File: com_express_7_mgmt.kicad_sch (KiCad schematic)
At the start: 66 parts, among them J1 Plug_Bus_CE7_EPT_401-51501-51, Q1 BSS138-7-F, Q2 BSS138-7-F, SW1 SW_1-1825027-1_THT, SW2 SW_1-1825027-1_THT, SW3 SW_DS04-254-1-01BK-SMT, U30 MAX16150A_SOT, U31 74AUP2G132, U32 TPS3840PL30DBVR, U33 74AUP2G132, U34 W25Q32FV_SOIC-8, U35 M24C64-F_DFN8

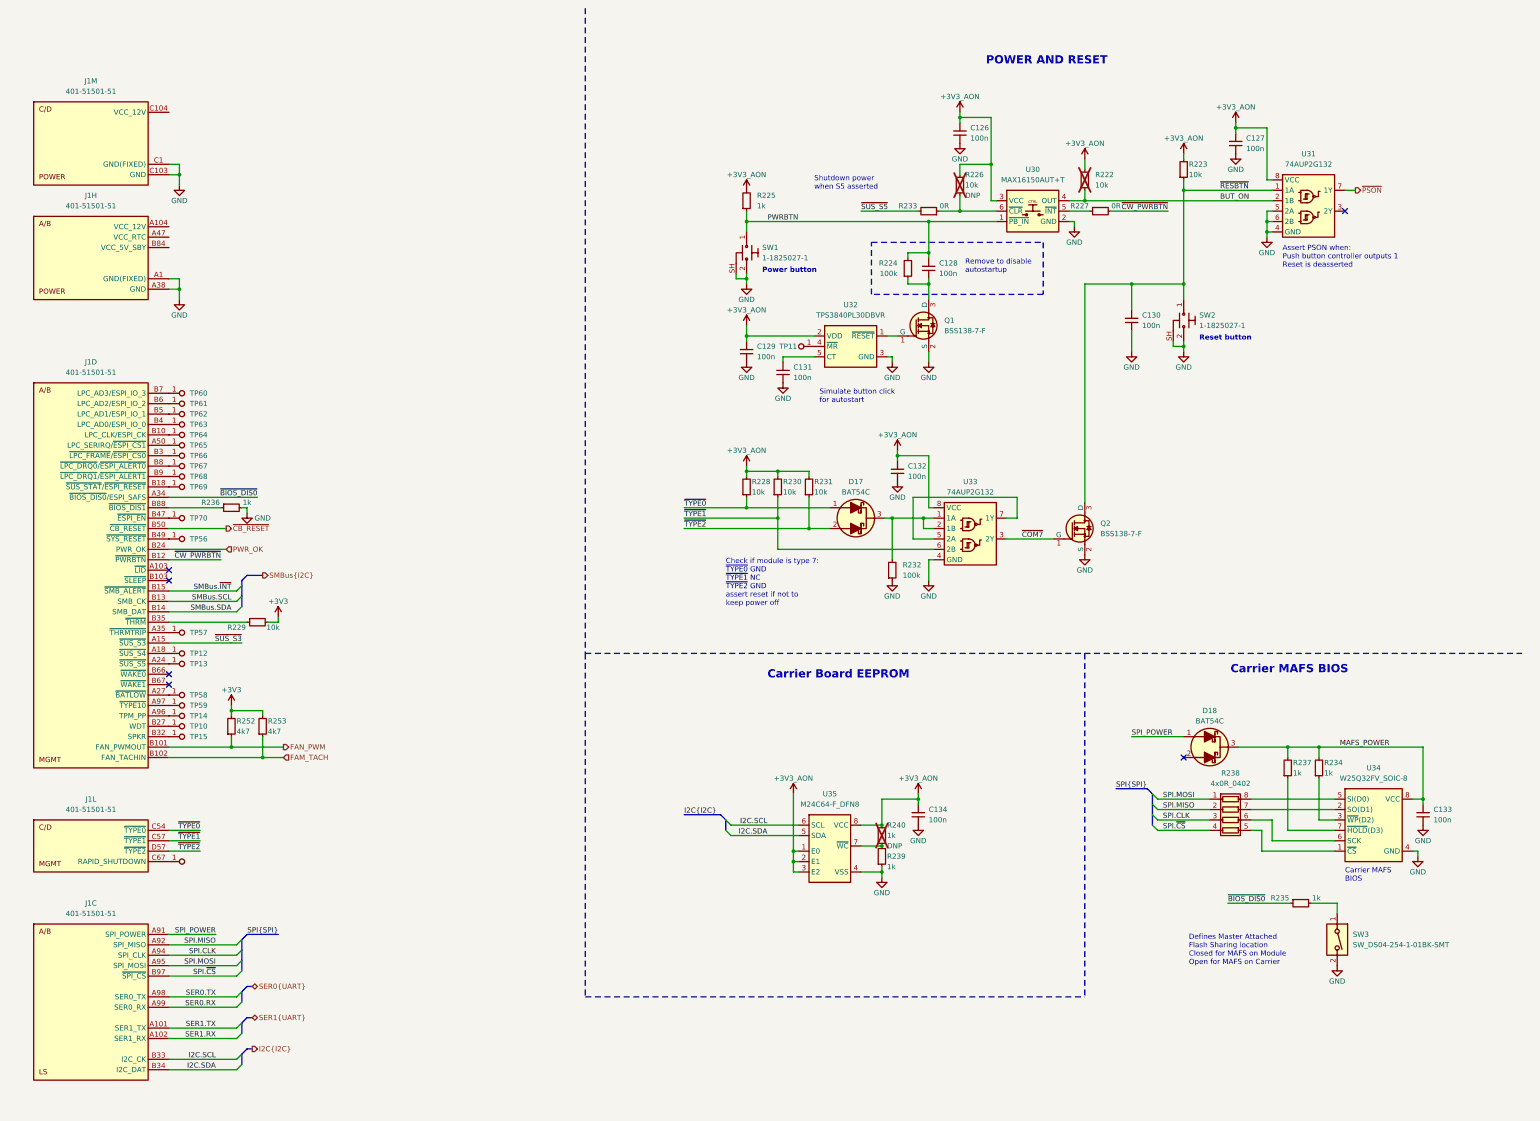
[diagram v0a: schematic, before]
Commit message: [#58137] Update backplane connector pinout
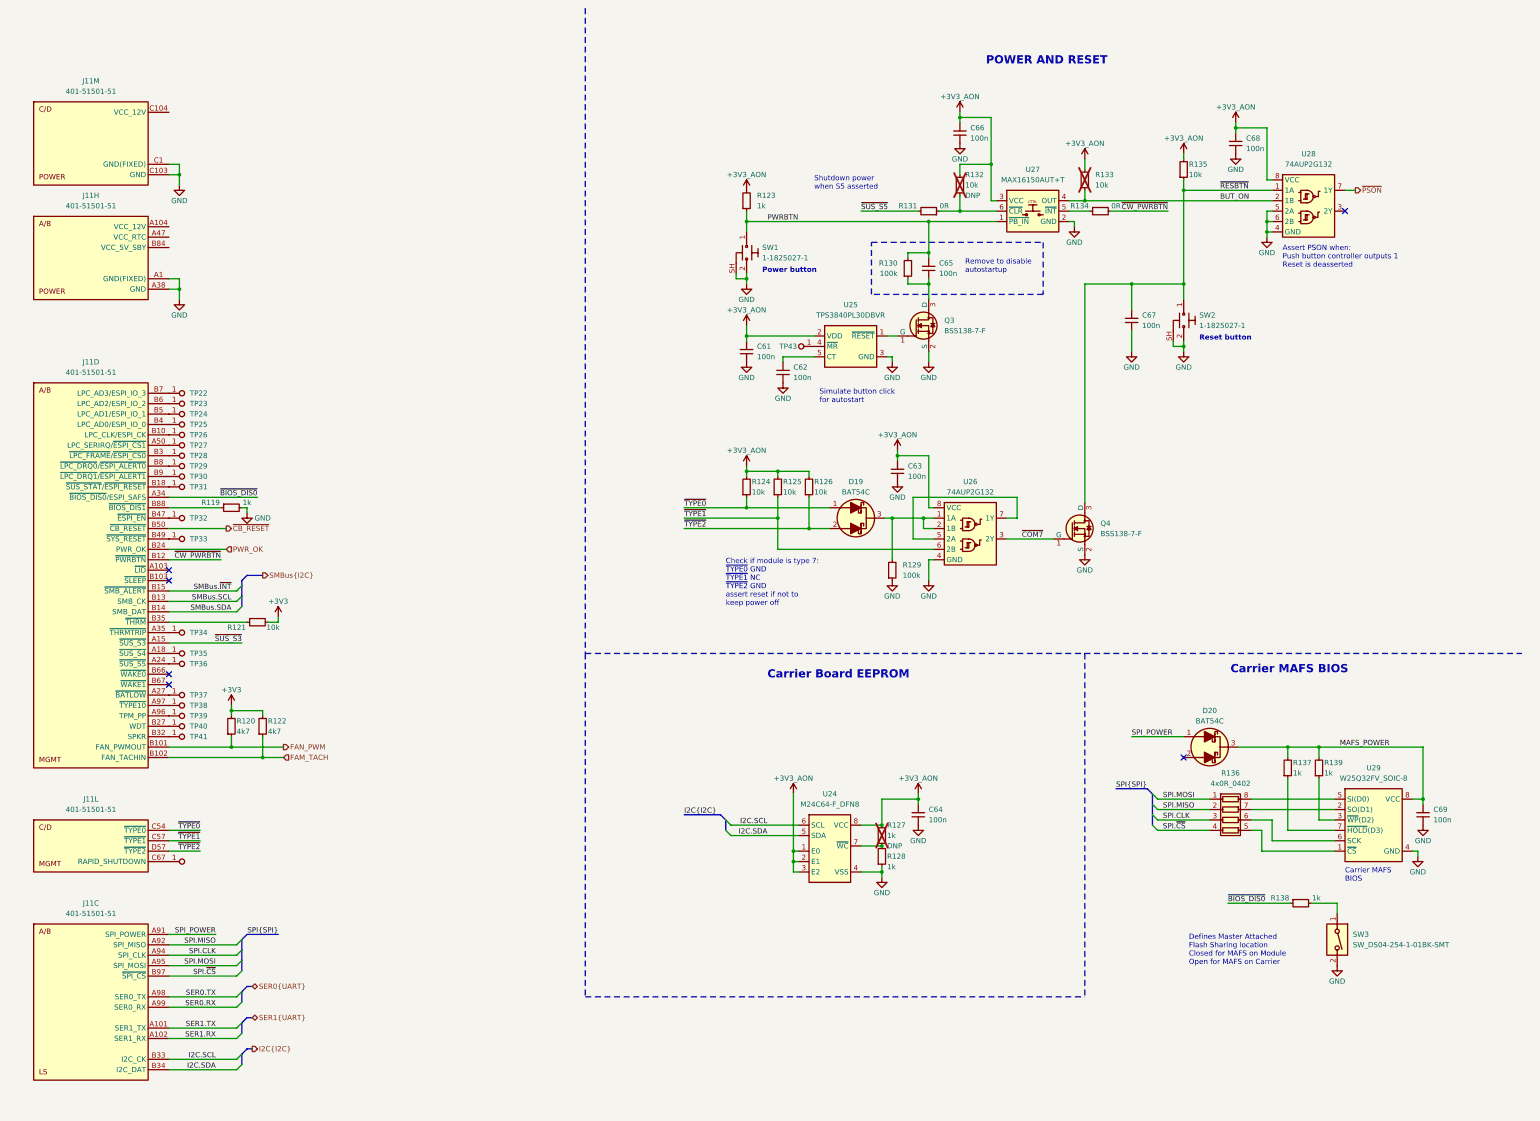
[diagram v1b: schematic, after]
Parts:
- renumbered C129 to C61, C131 to C62, C132 to C63, C134 to C64, C128 to C65, C126 to C66, C130 to C67, C127 to C68, C133 to C69, D17 to D19, D18 to D20, J1 to J11, Q1 to Q3, Q2 to Q4, R236 to R119, R252 to R120, R229 to R121, R253 to R122, R225 to R123, R228 to R124, R230 to R125, R231 to R126, R240 to R127, R239 to R128, R232 to R129, R224 to R130, R233 to R131, R226 to R132, R222 to R133, R227 to R134, R223 to R135, R238 to R136, R237 to R137, R235 to R138, R234 to R139, TP60 to TP22, TP61 to TP23, TP62 to TP24, TP63 to TP25, TP64 to TP26, TP65 to TP27, TP66 to TP28, TP67 to TP29, TP68 to TP30, TP69 to TP31, TP70 to TP32, TP56 to TP33, TP57 to TP34, TP12 to TP35, TP13 to TP36, TP58 to TP37, TP59 to TP38, TP14 to TP39, TP10 to TP40, TP15 to TP41, TP16 to TP42, TP11 to TP43, U35 to U24, U32 to U25, U33 to U26, U30 to U27, U31 to U28, U34 to U29

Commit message: [#58137] Add power sequencing and reset
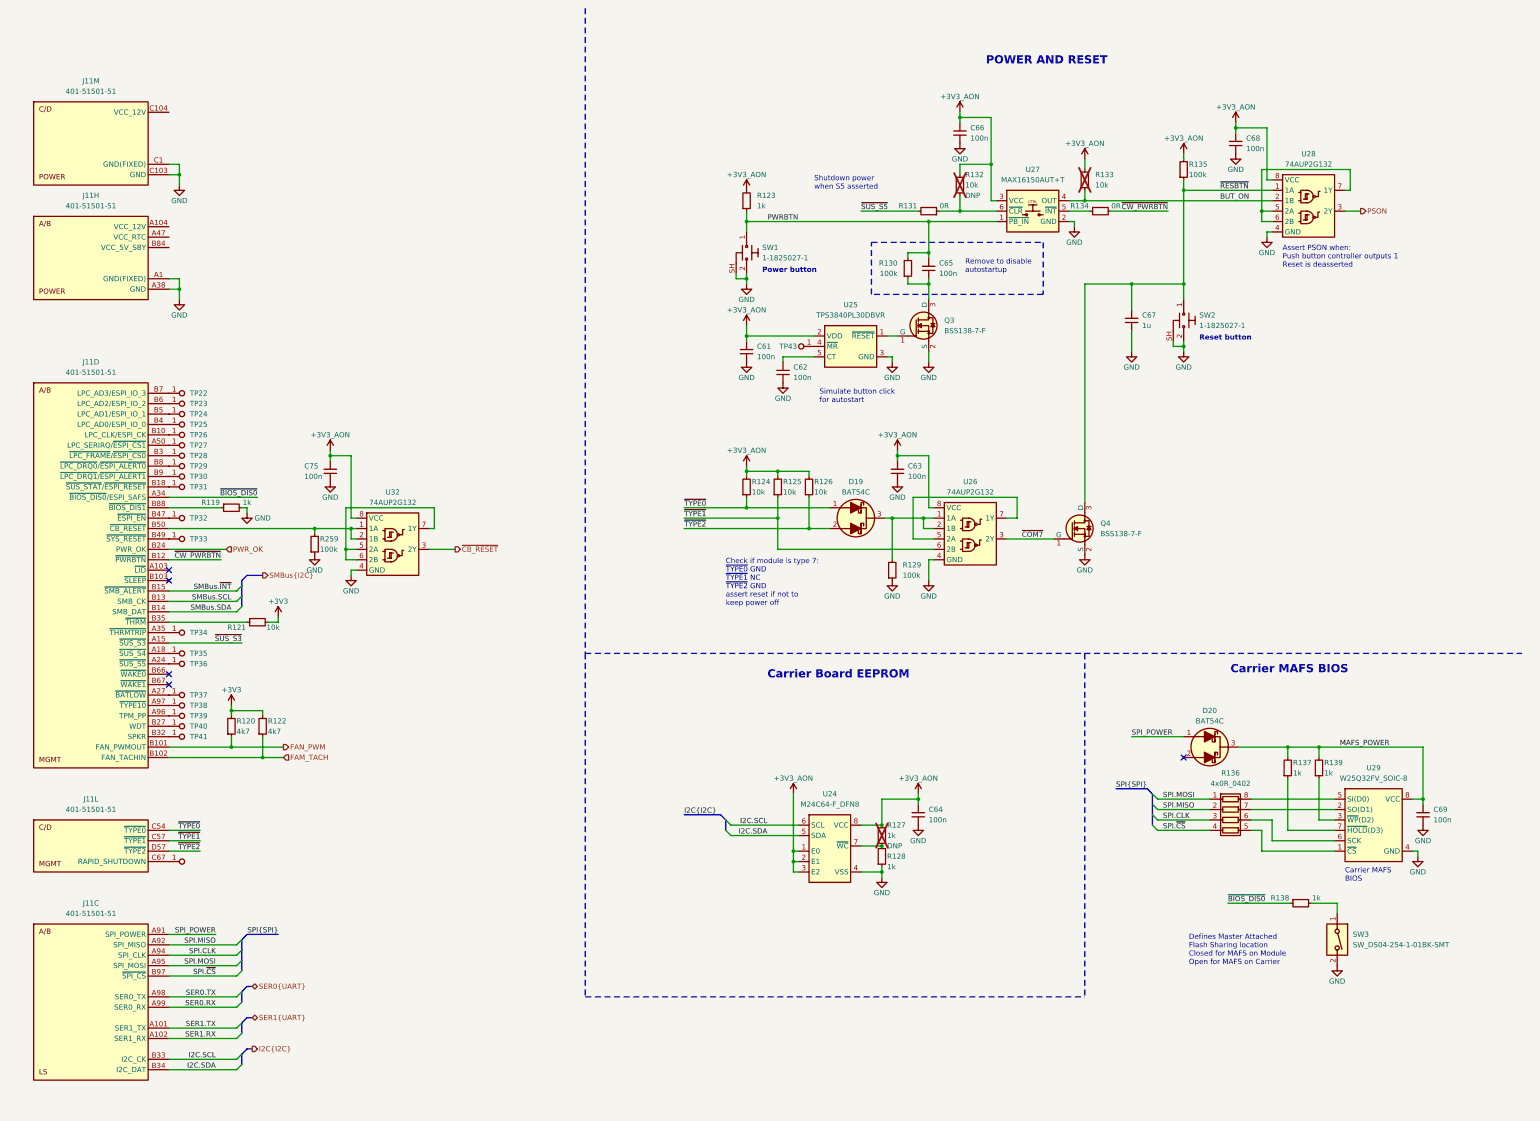
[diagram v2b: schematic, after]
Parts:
- removed C67: C_100n_0402, antmicro-footprints:C_0402_1005Metric, symbol antmicroCapacitors0402:C_100n_0402
- removed R135: R_10k_0402, antmicro-footprints:R_0402_1005Metric, symbol antmicroResistors0402:R_10k_0402
- added C67: C_1u_0402, antmicro-footprints:C_0402_1005Metric, symbol antmicroCapacitors0402:C_1u_0402
- added C75: C_100n_0402, antmicro-footprints:C_0402_1005Metric, symbol antmicroCapacitors0402:C_100n_0402
- added R135, R259: R_100k_0402, antmicro-footprints:R_0402_1005Metric, symbol antmicroResistors0402:R_100k_0402
- added U32: 74AUP2G132, antmicro-footprints:VSSOP-8_2.3x2mm_P0.5mm, symbol antmicroLogicGatesandInverters:74AUP2G132
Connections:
- net +3V3_AON: now also C75.2, R135.2, U32.8 (VCC)
- net GND: now also C67.1, C75.1, R259.1, U32.4 (GND); no longer U28.5 (2A), U28.6 (2B)
- net ~{CB_RESET}: now also U32.3 (2Y); no longer J11.B50 (~{CB_RESET})
- net ~{RESBTN}: now also C67.2, R135.1
- net PSON: now reaches U28.3 (2Y)
- net ~{PSON}: no longer names the net of U28.7 (1Y)
- net ~{PSON}: now also U28.5 (2A), U28.6 (2B)
- new net: J11.B50 (~{CB_RESET}), R259.2, U32.1 (1A), U32.2 (1B)
- new net: U32.5 (2A), U32.6 (2B), U32.7 (1Y)
- no-connect marks 6 -> 5

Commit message: [#58137] Connect SoM power rails
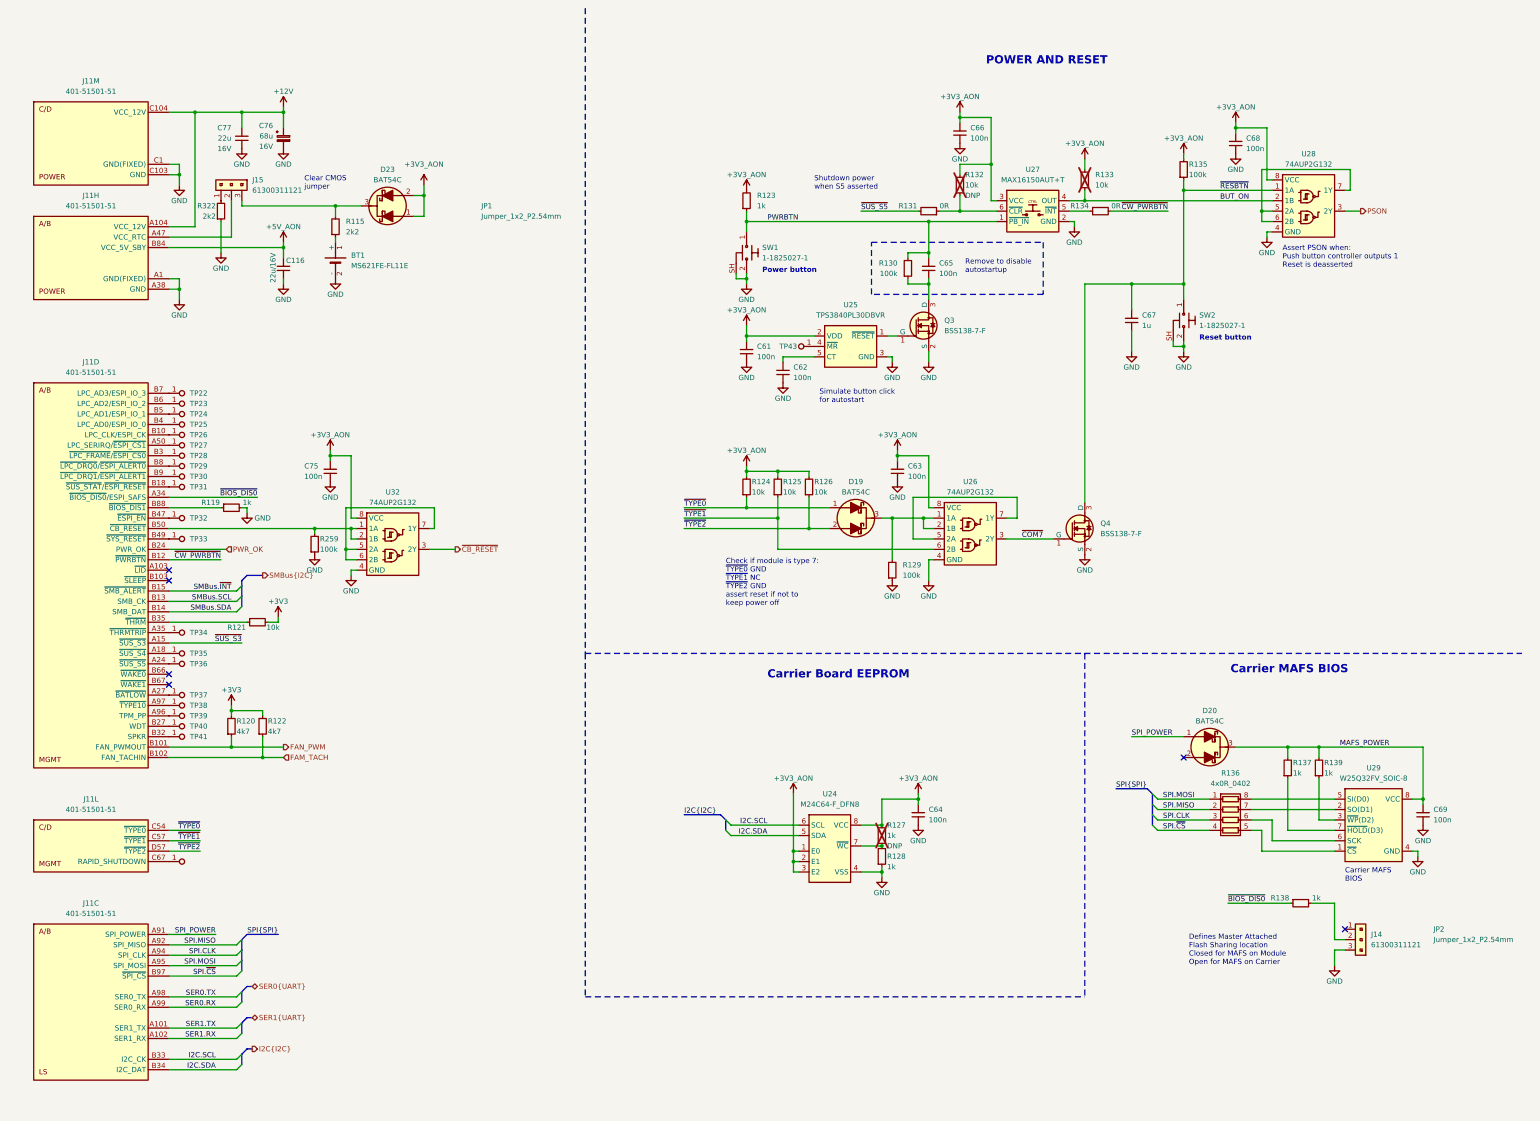
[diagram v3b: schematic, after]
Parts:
- removed SW3: SW_DS04-254-1-01BK-SMT, antmicro-footprints:SW_DS04-254-1-01BK-SMT, symbol antmicroSlideSwitches:SW_DS04-254-1-01BK-SMT
- added BT1: Battery_Holder_MS621FE-FL11E, antmicro-footprints:MS621FE-FL11E, symbol antmicroBatteryHoldersClipsContacts:Battery_Holder_MS621FE-FL11E
- added C116, C77: C_22u_16V_0603, antmicro-footprints:C_0603_1608Metric, symbol antmicroCapacitors0603:C_22u_16V_0603
- added C76: C_Pol_68u_16V_Panasonic-TQC-D, antmicro-footprints:C_Pol_EIA-D, symbol antmicroCapacitorspol:C_Pol_68u_16V_Panasonic-TQC-D
- added D23: BAT54C, antmicro-footprints:SOT-23-3, symbol antmicroDiodesRectifiersSingle:BAT54C
- added J14, J15: PinHeader_1x3_P2.54mm_Drill1.1mm, antmicro-footprints:PinHeader_1x3_P2.54mm_Drill1.1mm, symbol antmicroGenericPinHeaders:PinHeader_1x3_P2.54mm_Drill1.1mm
- added JP1, JP2: Jumper_1x2_P2.54mm, antmicro-footprints:Jumper_1x2_P2.54mm, symbol antmicroShuntsJumpers:Jumper_1x2_P2.54mm
- added R115, R322: R_2k2_0402, antmicro-footprints:R_0402_1005Metric, symbol antmicroResistors0402:R_2k2_0402
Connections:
- net +3V3_AON: now also D23.1, D23.2
- net GND: now also BT1.2 (-), C116.1, C76.2, C77.1, J14.3, R322.1
- net at R138.2: now also J14.2
- net +12V: now reaches J11.C104 (VCC_12V), J11.C105 (VCC_12V), J11.C106 (VCC_12V), J11.C107 (VCC_12V), J11.C108 (VCC_12V), J11.C109 (VCC_12V), J11.D104 (VCC_12V), J11.D105 (VCC_12V), J11.D106 (VCC_12V), J11.D107 (VCC_12V), J11.D108 (VCC_12V), J11.D109 (VCC_12V)
- net +12V: now also J11.A104 (VCC_12V), J11.A105 (VCC_12V), J11.A106 (VCC_12V), J11.A107 (VCC_12V), J11.A108 (VCC_12V), J11.A109 (VCC_12V), J11.B104 (VCC_12V), J11.B105 (VCC_12V), J11.B106 (VCC_12V), J11.B107 (VCC_12V), J11.B108 (VCC_12V), J11.B109 (VCC_12V), C76.1, C77.2
- net at J11.A47 (VCC_RTC): now also J15.2
- net +5V_AON: now reaches J11.B84 (VCC_5V_SBY), J11.B85 (VCC_5V_SBY), J11.B86 (VCC_5V_SBY), J11.B87 (VCC_5V_SBY)
- net +5V_AON: now also C116.2
- new net: BT1.1 (+), R115.1
- new net: J15.1, R322.2
- new net: D23.3, J15.3, R115.2
- no-connect marks 5 -> 6
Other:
- note added: "Clear CMOS jumper"
